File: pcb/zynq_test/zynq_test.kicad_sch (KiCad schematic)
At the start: 0 parts

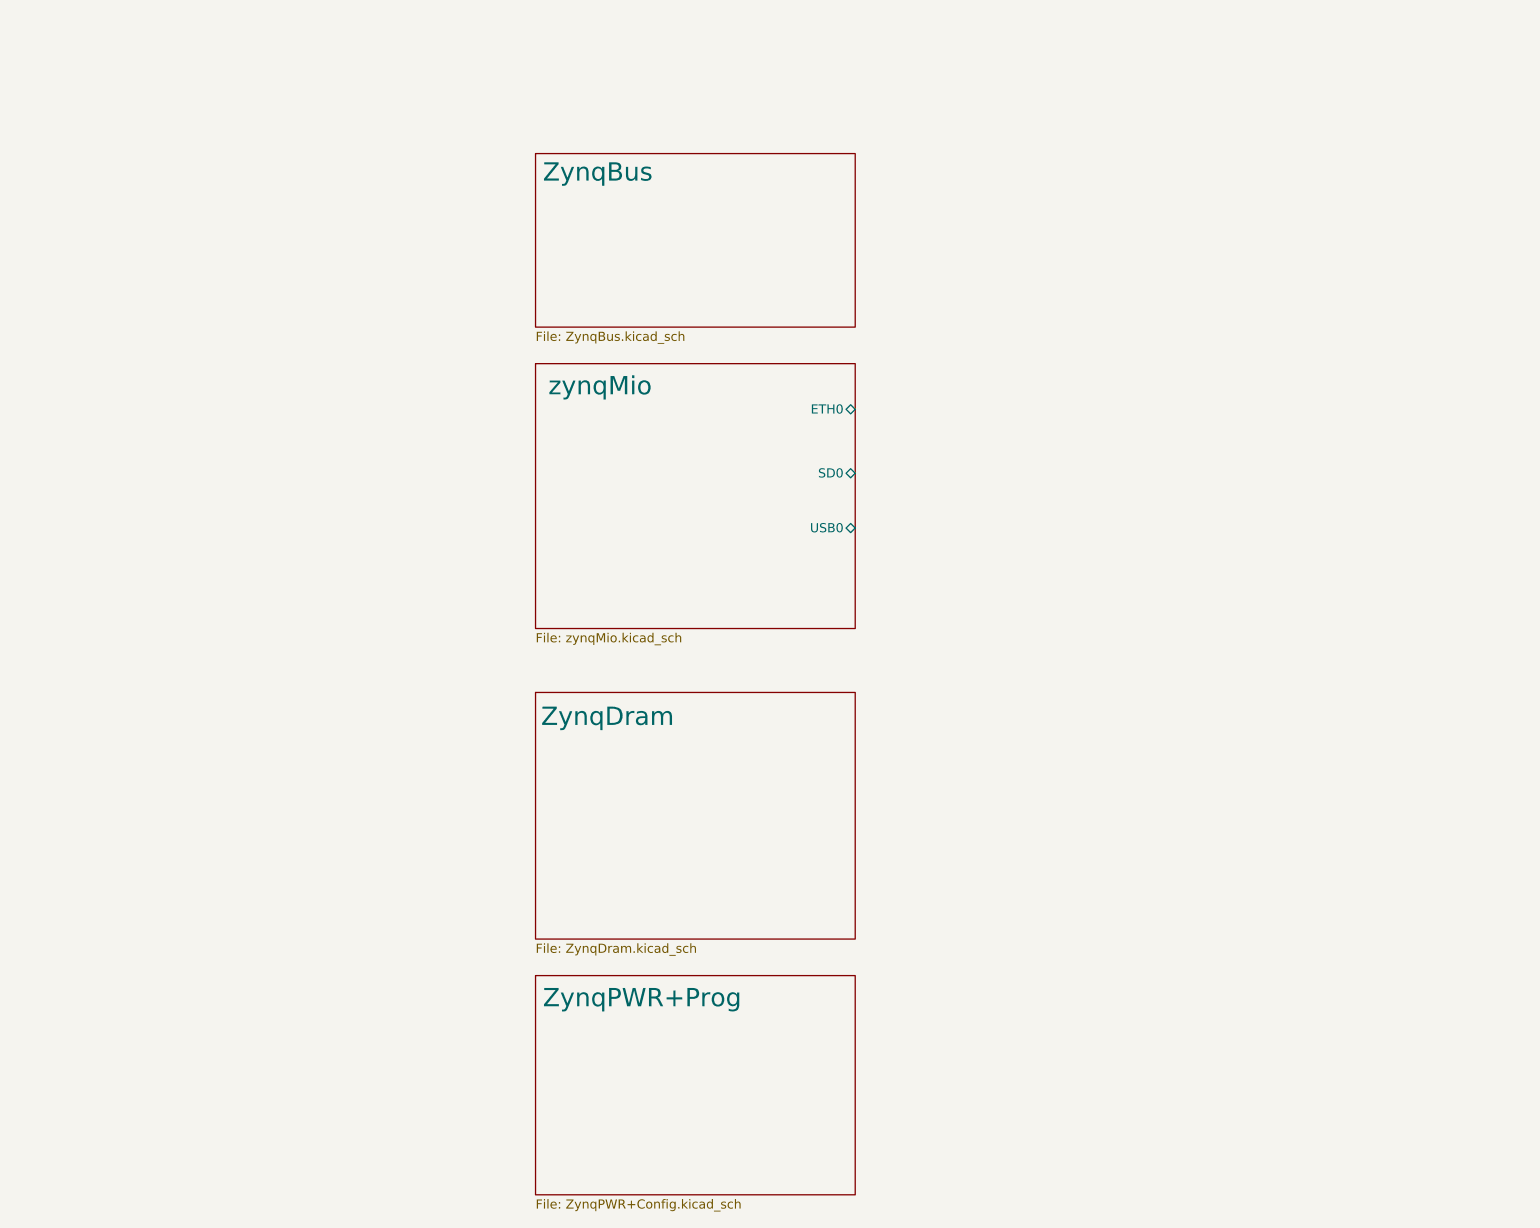
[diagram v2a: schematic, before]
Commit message: Finished FPGA decouploing, and jtag programmer
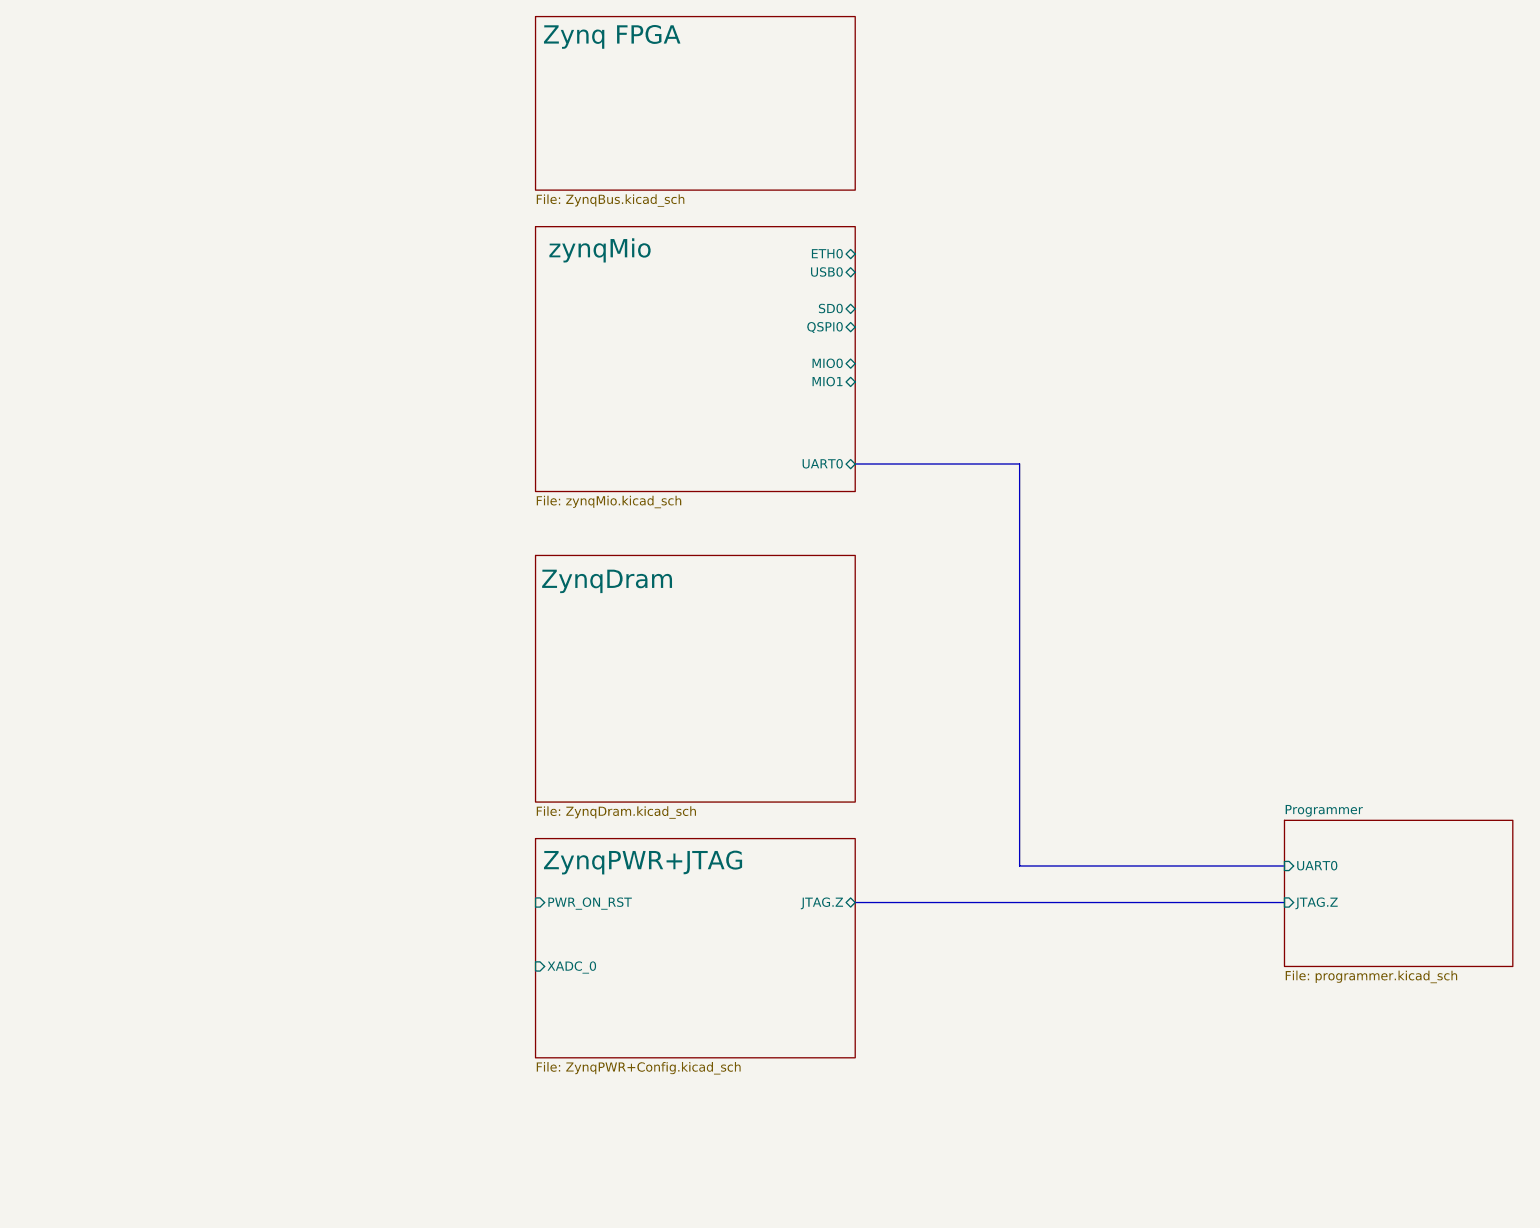
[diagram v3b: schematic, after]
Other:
- sheet ZynqBus renamed Zynq FPGA
- sheet ZynqPWR+Prog renamed ZynqPWR+JTAG
- added sheet Programmer (programmer.kicad_sch)
- sheet ZynqPWR+JTAG ports: added JTAG.Z, PWR_ON_RST, XADC_0; removed none
- sheet zynqMio ports: added MIO0, MIO1, QSPI0, UART0; removed none
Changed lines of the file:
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@@
 	(generator_version "9.0")
 	(paper "A4")
-	(sheet
-		(at 105.41 148.59)
+	(bus
+		(pts
+			(xy 172.72 77.47) (xy 149.86 77.47)
+		)
+		(stroke
+			(width 0)
+			(type default)
+		)
+	)
+	(bus
+		(pts
+			(xy 172.72 133.35) (xy 172.72 77.47)
+		)
+		(stroke
+			(width 0)
+			(type default)
+		)
+	)
+	(bus
+		(pts
+			(xy 149.86 138.43) (xy 209.55 138.43)
+		)
+		(stroke
+			(width 0)
+			(type default)
+		)
+	)
+	(bus
+		(pts
+			(xy 209.55 133.35) (xy 172.72 133.35)
+		)
+		(stroke
+			(width 0)
+			(type default)
+		)
+	)
+	(sheet
+		(at 105.41 129.54)
 		(size 44.45 30.48)
 		(exclude_from_sim no)
@@
 			(color 0 0 0 0.0000)
 		)
-		(property "Sheetname" "ZynqPWR+Prog"
-			(at 106.426 153.162 0)
+		(property "Sheetname" "ZynqPWR+JTAG"
+			(at 106.426 134.112 0)
 			(effects
 				(font
@@
 		)
 		(property "Sheetfile" "ZynqPWR+Config.kicad_sch"
-			(at 105.41 179.6546 0)
-			(effects
-				(font
-					(size 1.27 1.27)
-				)
-				(justify left top)
+			(at 105.41 160.6046 0)
+			(effects
+				(font
+					(size 1.27 1.27)
+				)
+				(justify left top)
+			)
+		)
+		(pin "JTAG.Z" bidirectional
+			(at 149.86 138.43 0)
+			(effects
+				(font
+					(size 1.27 1.27)
+				)
+				(justify right)
+			)
+		)
+		(pin "PWR_ON_RST" input
+			(at 105.41 138.43 180)
+			(effects
+				(font
+					(size 1.27 1.27)
+				)
+				(justify left)
+			)
+		)
+		(pin "XADC_0" input
+			(at 105.41 147.32 180)
+			(effects
+				(font
+					(size 1.27 1.27)
+				)
+				(justify left)
 			)
 		)
@@
 	)
 	(sheet
-		(at 105.41 109.22)
+		(at 105.41 90.17)
 		(size 44.45 34.29)
 		(exclude_from_sim no)
@@
 		)
 		(property "Sheetname" "ZynqDram"
-			(at 106.172 114.046 0)
+			(at 106.172 94.996 0)
 			(effects
 				(font
@@
 		)
 		(property "Sheetfile" "ZynqDram.kicad_sch"
-			(at 105.41 144.0946 0)
+			(at 105.41 125.0446 0)
 			(effects
 				(font
@@
 	)
 	(sheet
-		(at 105.41 34.29)
+		(at 105.41 15.24)
 		(size 44.45 24.13)
 		(exclude_from_sim no)
@@
 			(color 0 0 0 0.0000)
 		)
-		(property "Sheetname" "ZynqBus"
-			(at 106.426 38.354 0)
+		(property "Sheetname" "Zynq FPGA"
+			(at 106.426 19.304 0)
 			(effects
 				(font
@@
 		)
 		(property "Sheetfile" "ZynqBus.kicad_sch"
-			(at 105.41 59.0046 0)
+			(at 105.41 39.9546 0)
 			(effects
 				(font
@@
 	)
 	(sheet
-		(at 105.41 63.5)
+		(at 209.55 127)
+		(size 31.75 20.32)
+		(exclude_from_sim no)
+		(in_bom yes)
+		(on_board yes)
+		(dnp no)
+		(fields_autoplaced yes)
+		(stroke
+			(width 0.1524)
+			(type solid)
+		)
+		(fill
+			(color 0 0 0 0.0000)
+		)
+		(property "Sheetname" "Programmer"
+			(at 209.55 126.2884 0)
+			(effects
+				(font
+					(size 1.27 1.27)
+				)
+				(justify left bottom)
+			)
+		)
+		(property "Sheetfile" "programmer.kicad_sch"
+			(at 209.55 147.9046 0)
+			(effects
+				(font
+					(size 1.27 1.27)
+				)
+				(justify left top)
+			)
+		)
+		(pin "JTAG.Z" input
+			(at 209.55 138.43 180)
+			(effects
+				(font
+					(size 1.27 1.27)
+				)
+				(justify left)
+			)
+		)
+		(pin "UART0" input
+			(at 209.55 133.35 180)
+			(effects
+				(font
+					(size 1.27 1.27)
+				)
+				(justify left)
+			)
+		)
+		(instances
+			(project "zynq_test"
+				(path "/0637578d-4ce5-4d31-b973-2de977269ea5"
+					(page "6")
+				)
+			)
+		)
+	)
+	(sheet
+		(at 105.41 44.45)
 		(size 44.45 36.83)
 		(exclude_from_sim no)
@@
 		)
 		(property "Sheetname" "zynqMio"
-			(at 107.188 68.072 0)
+			(at 107.188 49.022 0)
 			(effects
 				(font
@@
 		)
 		(property "Sheetfile" "zynqMio.kicad_sch"
-			(at 105.41 100.9146 0)
+			(at 105.41 81.8646 0)
 			(effects
 				(font
@@
 		)
 		(pin "ETH0" bidirectional
-			(at 149.86 69.85 0)
+			(at 149.86 48.26 0)
 			(effects
 				(font
@@
 		)
 		(pin "SD0" bidirectional
-			(at 149.86 78.74 0)
+			(at 149.86 55.88 0)
 			(effects
 				(font
@@
 		)
 		(pin "USB0" bidirectional
-			(at 149.86 86.36 0)
-			(effects
-				(font
+			(at 149.86 50.8 0)
+			(effects
+				(font
+					(size 1.27 1.27)
+				)
+				(justify right)
+			)
+		)
+		(pin "MIO0" bidirectional
+			(at 149.86 63.5 0)
+			(effects
+				(font
+					(size 1.27 1.27)
+				)
+				(justify right)
+			)
+		)
+		(pin "MIO1" bidirectional
+			(at 149.86 66.04 0)
+			(effects
+				(font
+					(size 1.27 1.27)
+				)
+				(justify right)
+			)
+		)
+		(pin "QSPI0" bidirectional
+			(at 149.86 58.42 0)
+			(effects
+				(font
+					(size 1.27 1.27)
+				)
+				(justify right)
+			)
+		)
+		(pin "UART0" bidirectional
+			(at 149.86 77.47 0)
+			(effects
+				(font

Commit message: Finished boot media, added structure for IO
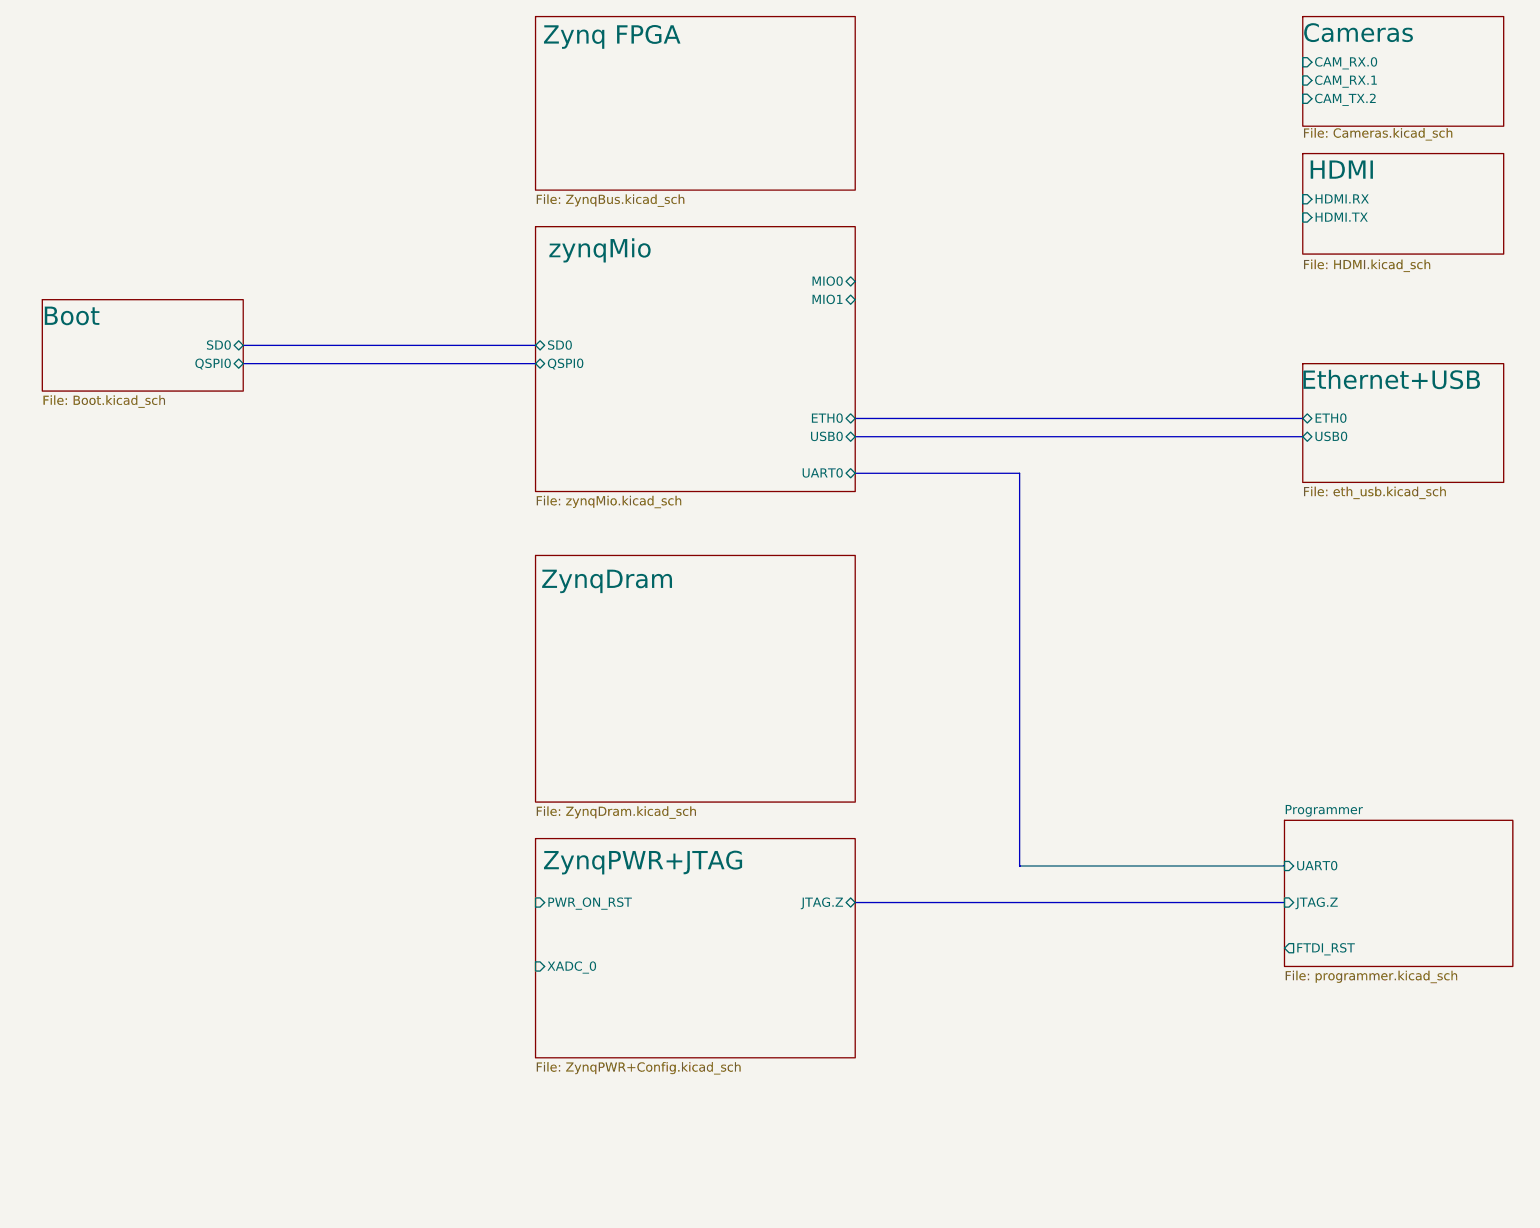
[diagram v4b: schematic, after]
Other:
- added sheet Boot (Boot.kicad_sch)
- added sheet Cameras (Cameras.kicad_sch)
- added sheet Ethernet+USB (eth_usb.kicad_sch)
- added sheet HDMI (HDMI.kicad_sch)
- sheet Programmer ports: added FTDI_RST; removed none

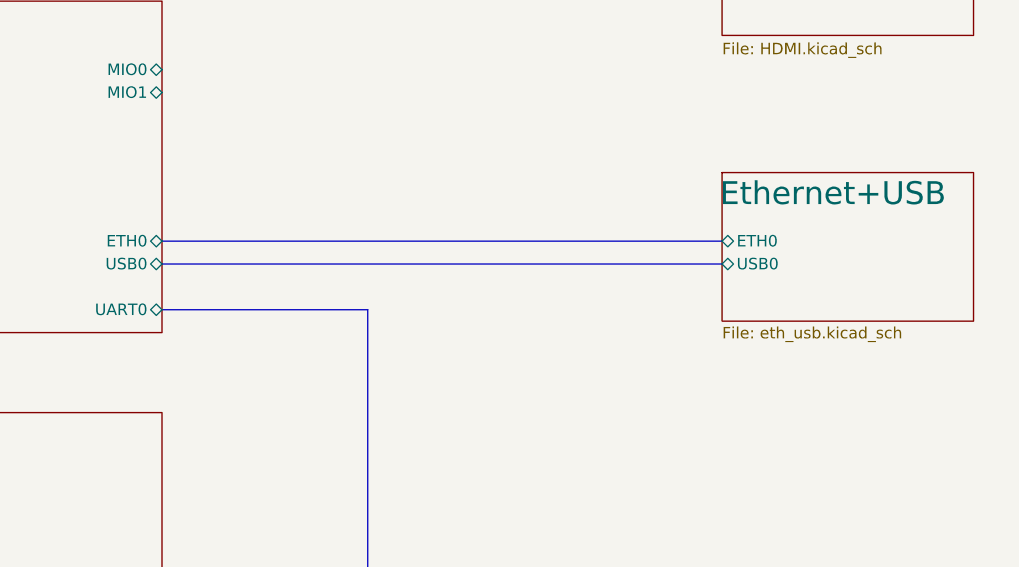
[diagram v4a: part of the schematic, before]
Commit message: Finished USB, started om ETH PHY
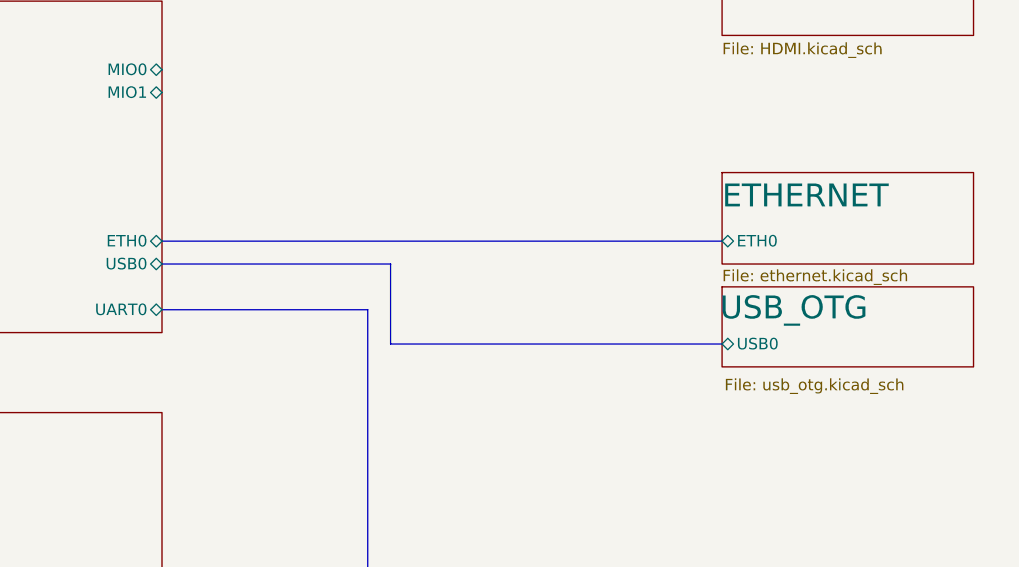
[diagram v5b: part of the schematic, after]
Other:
- sheet Ethernet+USB renamed USB_OTG
- added sheet ETHERNET (ethernet.kicad_sch)
- sheet USB_OTG: file eth_usb.kicad_sch -> usb_otg.kicad_sch
- sheet USB_OTG ports: added none; removed ETH0
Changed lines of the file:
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@@
+	(bus
+		(pts
+			(xy 175.26 82.55) (xy 175.26 73.66)
+		)
+		(stroke
+			(width 0)
+			(type default)
+		)
+	)
 	(bus
 		(pts
@@
 	(bus
 		(pts
+			(xy 149.86 138.43) (xy 209.55 138.43)
+		)
+		(stroke
+			(width 0)
+			(type default)
+		)
+	)
+	(bus
+		(pts
 			(xy 149.86 71.12) (xy 212.09 71.12)
 		)
@@
 	(bus
 		(pts
-			(xy 149.86 138.43) (xy 209.55 138.43)
-		)
-		(stroke
-			(width 0)
-			(type default)
-		)
-	)
-	(bus
-		(pts
-			(xy 149.86 73.66) (xy 212.09 73.66)
+			(xy 175.26 73.66) (xy 149.86 73.66)
+		)
+		(stroke
+			(width 0)
+			(type default)
+		)
+	)
+	(bus
+		(pts
+			(xy 175.26 82.55) (xy 212.09 82.55)
 		)
 		(stroke
@@
 	)
 	(sheet
+		(at 212.09 63.5)
+		(size 27.94 10.16)
+		(exclude_from_sim no)
+		(in_bom yes)
+		(on_board yes)
+		(dnp no)
+		(stroke
+			(width 0.1524)
+			(type solid)
+		)
+		(fill
+			(color 0 0 0 0.0000)
+		)
+		(property "Sheetname" "ETHERNET"
+			(at 212.09 67.564 0)
+			(effects
+				(font
+					(size 2.54 2.54)
+				)
+				(justify left bottom)
+			)
+		)
+		(property "Sheetfile" "ethernet.kicad_sch"
+			(at 212.09 74.2446 0)
+			(effects
+				(font
+					(size 1.27 1.27)
+				)
+				(justify left top)
+			)
+		)
+		(pin "ETH0" bidirectional
+			(at 212.09 71.12 180)
+			(effects
+				(font
+					(size 1.27 1.27)
+				)
+				(justify left)
+			)
+		)
+		(instances
+			(project "zynq_test"
+				(path "/0637578d-4ce5-4d31-b973-2de977269ea5"
+					(page "11")
+				)
+			)
+		)
+	)
+	(sheet
 		(at 105.41 15.24)
 		(size 44.45 24.13)
@@
 	)
 	(sheet
-		(at 212.09 63.5)
-		(size 27.94 16.51)
-		(exclude_from_sim no)
-		(in_bom yes)
-		(on_board yes)
-		(dnp no)
-		(stroke
-			(width 0.1524)
-			(type solid)
-		)
-		(fill
-			(color 0 0 0 0.0000)
-		)
-		(property "Sheetname" "Ethernet+USB"
-			(at 211.836 67.31 0)
-			(effects
-				(font
-					(size 2.54 2.54)
-				)
-				(justify left bottom)
-			)
-		)
-		(property "Sheetfile" "eth_usb.kicad_sch"
-			(at 212.09 80.5946 0)
-			(effects
-				(font
-					(size 1.27 1.27)
-				)
-				(justify left top)
-			)
-		)
-		(pin "ETH0" bidirectional
-			(at 212.09 71.12 180)
-			(effects
-				(font
-					(size 1.27 1.27)
-				)
-				(justify left)
+		(at 212.09 76.2)
+		(size 27.94 8.89)
+		(exclude_from_sim no)
+		(in_bom yes)
+		(on_board yes)
+		(dnp no)
+		(stroke
+			(width 0.1524)
+			(type solid)
+		)
+		(fill
+			(color 0 0 0 0.0000)
+		)
+		(property "Sheetname" "USB_OTG"
+			(at 211.836 80.01 0)
+			(effects
+				(font
+					(size 2.54 2.54)
+				)
+				(justify left bottom)
+			)
+		)
+		(property "Sheetfile" "usb_otg.kicad_sch"
+			(at 212.344 86.36 0)
+			(effects
+				(font
+					(size 1.27 1.27)
+				)
+				(justify left top)
 			)
 		)
 		(pin "USB0" bidirectional
-			(at 212.09 73.66 180)
-			(effects
-				(font
+			(at 212.09 82.55 180)
+			(effects
+				(font
